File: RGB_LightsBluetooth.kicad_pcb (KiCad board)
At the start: 2 copper layers, 87.5 x 42.8 mm, 27 parts, among them J1 1935161, J2 1935161, J3 1935161, J4 HC-05, Q1 BC548, Q2 BC548, Q3 BC548, Q4 IRF9640, Q5 IRF9640, Q6 IRF9640, SW1 SW_DPST, U2 ATtiny2313-20P

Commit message: pcb without route
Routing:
- net GND: track 176.8 -> 0.00 mm
- net /12V: track 65.9 -> 0.00 mm
- net /5V: track 40.1 -> 0.00 mm
- net Net-(Q2-Pad1): track 26.3 -> 0.00 mm
- net Net-(Q1-Pad1): track 25.1 -> 0.00 mm
- net Net-(Q3-Pad1): track 24.9 -> 0.00 mm
- net Net-(J2-Pad1): track 21.6 -> 0.00 mm, vias 1 -> 0
- net Net-(J3-Pad1): track 21.1 -> 0.00 mm, vias 1 -> 0
- net Net-(J1-Pad1): track 20.6 -> 0.00 mm
- net /TX: track 18.5 -> 0.00 mm
- net Net-(J1-Pad2): track 17.9 -> 0.00 mm
- net /RX: track 17.5 -> 0.00 mm
- net Net-(R3-Pad2): track 14.3 -> 0.00 mm
- net Net-(Q1-Pad2): track 13.8 -> 0.00 mm
- net Net-(Q2-Pad2): track 13.1 -> 0.00 mm
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
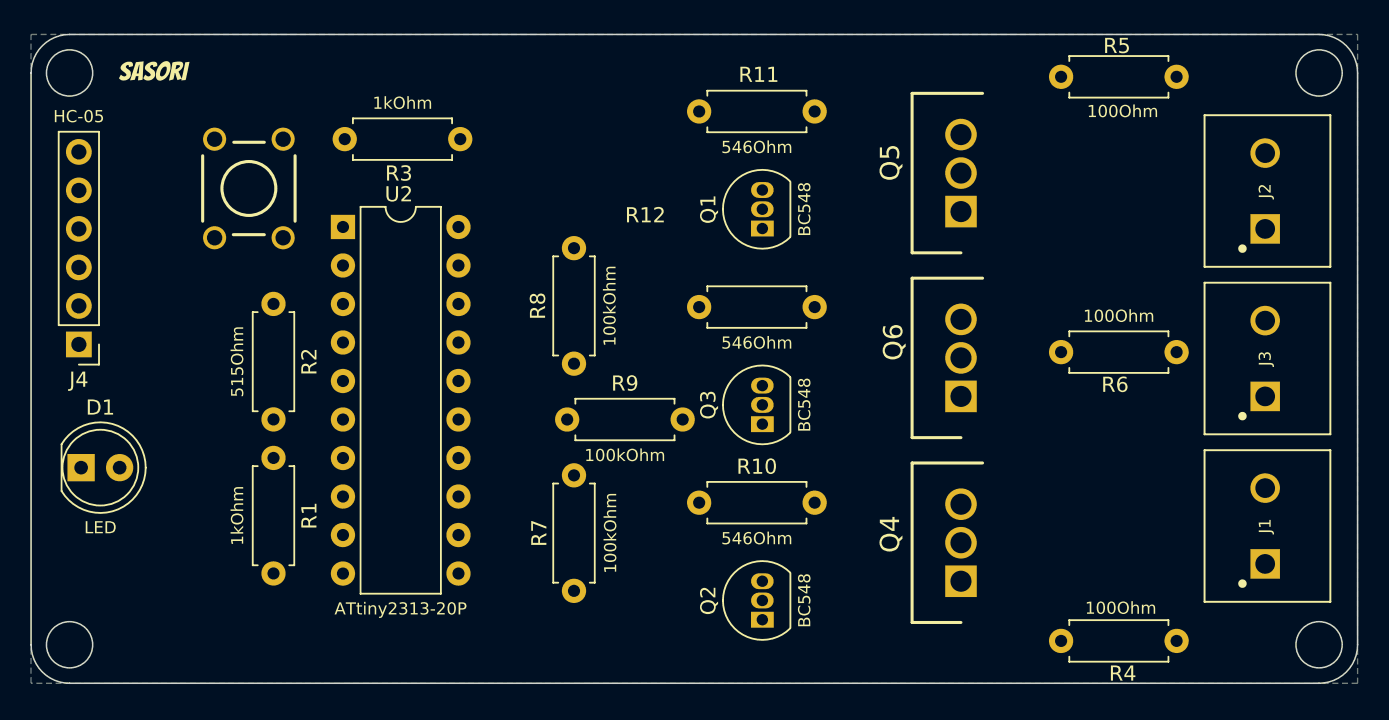
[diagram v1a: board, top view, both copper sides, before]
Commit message: pcb autorouting
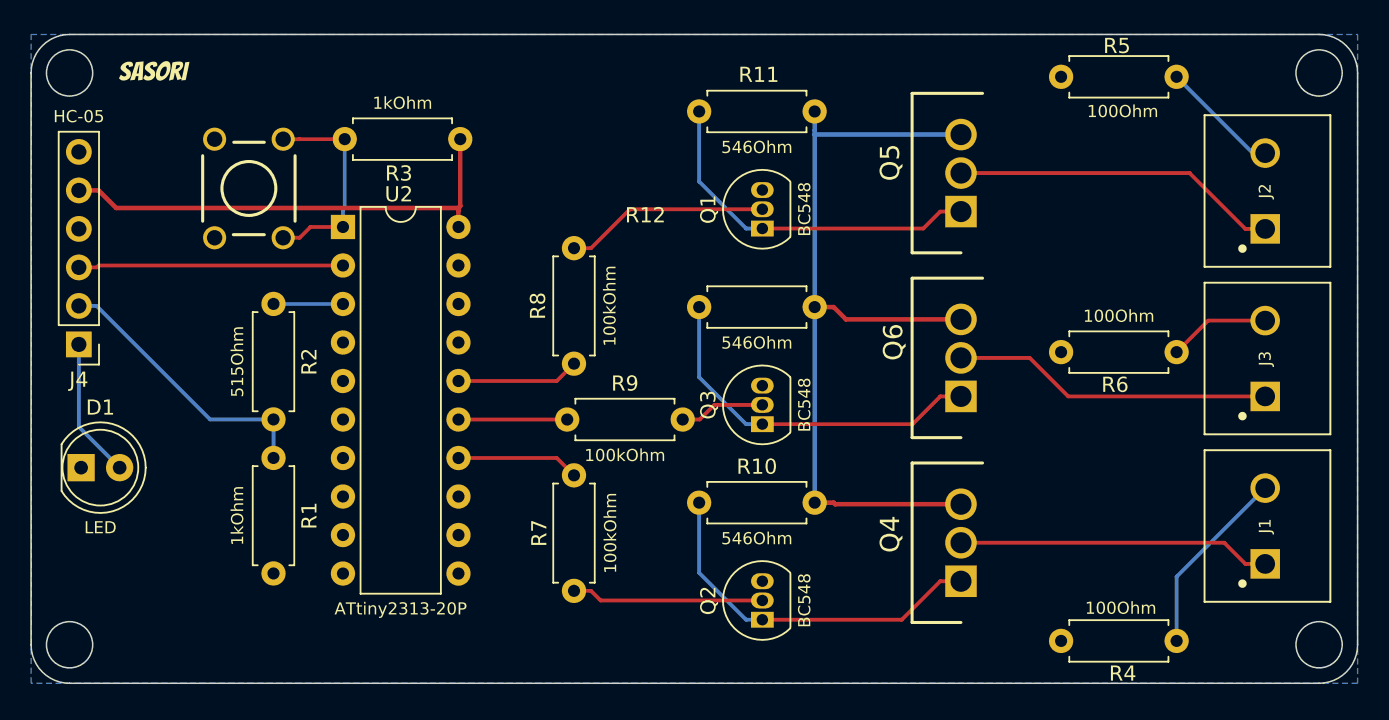
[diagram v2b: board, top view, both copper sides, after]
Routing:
- net /12V: track 0.00 -> 55.1 mm
- net /5V: track 0.00 -> 31.4 mm
- net Net-(Q2-Pad1): track 0.00 -> 24.2 mm
- net Net-(Q3-Pad1): track 0.00 -> 23.9 mm
- net Net-(Q1-Pad1): track 0.00 -> 23.6 mm
- net Net-(J2-Pad1): track 0.00 -> 21.6 mm
- net Net-(J3-Pad1): track 0.00 -> 21.1 mm
- net Net-(J1-Pad1): track 0.00 -> 20.6 mm
- net /TX: track 0.00 -> 18.5 mm
- net /RX: track 0.00 -> 17.5 mm
- net Net-(R3-Pad2): track 0.00 -> 14.1 mm
- net Net-(Q1-Pad2): track 0.00 -> 13.5 mm
- net Net-(Q2-Pad2): track 0.00 -> 12.7 mm
- net Net-(J1-Pad2): track 0.00 -> 12.5 mm
- net Net-(D1-Pad2): track 0.00 -> 9.24 mm
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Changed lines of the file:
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@@
     (style (thickness 0.1) (arrow_length 1.27) (text_position_mode 0) (extension_height 0.58642) (extension_offset 0.5) keep_text_aligned)
   )
+  (segment (start 136.261 71.9288) (end 133.2893 71.9288) (width 0.25) (layer "F.Cu") (net 2))
+  (segment (start 136.144 77.724) (end 133.9965 77.724) (width 0.25) (layer "F.Cu") (net 2))
+  (segment (start 132.198 71.9328) (end 133.2853 71.9328) (width 0.25) (layer "F.Cu") (net 2))
+  (segment (start 133.9965 77.724) (end 133.2853 78.4352) (width 0.25) (layer "F.Cu") (net 2))
+  (segment (start 133.2893 71.9288) (end 133.2853 71.9328) (width 0.25) (layer "F.Cu") (net 2))
+  (segment (start 132.198 78.4352) (end 133.2853 78.4352) (width 0.25) (layer "F.Cu") (net 2))
+  (segment (start 136.144 76.5987) (end 136.261 76.4817) (width 0.25) (layer "B.Cu") (net 2))
+  (segment (start 136.261 76.4817) (end 136.261 71.9288) (width 0.25) (layer "B.Cu") (net 2))
+  (segment (start 136.144 77.724) (end 136.144 76.5987) (width 0.25) (layer "B.Cu") (net 2))
+  (segment (start 118.722 82.931) (end 119.8973 82.931) (width 0.25) (layer "B.Cu") (net 3))
+  (segment (start 131.562 90.419) (end 127.3853 90.419) (width 0.25) (layer "B.Cu") (net 3))
+  (segment (start 131.562 90.419) (end 131.562 92.959) (width 0.25) (layer "B.Cu") (net 3))
+  (segment (start 127.3853 90.419) (end 119.8973 82.931) (width 0.25) (layer "B.Cu") (net 3))
+  (segment (start 131.567 82.804) (end 131.562 82.799) (width 0.25) (layer "B.Cu") (net 4))
+  (segment (start 136.144 82.804) (end 131.567 82.804) (width 0.25) (layer "B.Cu") (net 4))
+  (segment (start 143.881 76.3566) (end 143.881 71.9288) (width 0.3) (layer "F.Cu") (net 5))
+  (segment (start 118.722 75.311) (end 120.0223 75.311) (width 0.3) (layer "F.Cu") (net 5))
+  (segment (start 143.764 76.4736) (end 121.1849 76.4736) (width 0.3) (layer "F.Cu") (net 5))
+  (segment (start 143.764 77.724) (end 143.764 76.6238) (width 0.3) (layer "F.Cu") (net 5))
+  (segment (start 143.764 76.6238) (end 143.764 76.4736) (width 0.3) (layer "F.Cu") (net 5))
+  (segment (start 143.764 76.4736) (end 143.881 76.3566) (width 0.3) (layer "F.Cu") (net 5))
+  (segment (start 121.1849 76.4736) (end 120.0223 75.311) (width 0.3) (layer "F.Cu") (net 5))
+  (segment (start 196.977 94.949) (end 191.135 100.791) (width 0.25) (layer "B.Cu") (net 6))
+  (segment (start 191.135 100.791) (end 191.135 105.029) (width 0.25) (layer "B.Cu") (net 6))
+  (segment (start 196.168 72.851) (end 191.135 67.818) (width 0.25) (layer "B.Cu") (net 7))
+  (segment (start 196.977 72.851) (end 196.168 72.851) (width 0.25) (layer "B.Cu") (net 7))
+  (segment (start 196.977 83.9) (end 193.214 83.9) (width 0.25) (layer "F.Cu") (net 8))
+  (segment (start 193.214 83.9) (end 191.135 85.979) (width 0.25) (layer "F.Cu") (net 8))
+  (segment (start 143.764 92.964) (end 150.241 92.964) (width 0.25) (layer "F.Cu") (net 9))
+  (segment (start 150.241 92.964) (end 151.384 94.107) (width 0.25) (layer "F.Cu") (net 9))
+  (segment (start 153.1443 102.362) (end 152.5093 101.727) (width 0.25) (layer "F.Cu") (net 10))
+  (segment (start 151.384 101.727) (end 152.5093 101.727) (width 0.25) (layer "F.Cu") (net 10))
+  (segment (start 163.809 102.362) (end 153.1443 102.362) (width 0.25) (layer "F.Cu") (net 10))
+  (segment (start 143.764 87.884) (end 150.241 87.884) (width 0.25) (layer "F.Cu") (net 11))
+  (segment (start 150.241 87.884) (end 151.384 86.741) (width 0.25) (layer "F.Cu") (net 11))
+  (segment (start 151.384 79.121) (end 152.5093 79.121) (width 0.25) (layer "F.Cu") (net 12))
+  (segment (start 163.809 76.5556) (end 155.0747 76.5556) (width 0.25) (layer "F.Cu") (net 12))
+  (segment (start 155.0747 76.5556) (end 152.5093 79.121) (width 0.25) (layer "F.Cu") (net 12))
+  (segment (start 143.764 90.424) (end 150.934 90.424) (width 0.25) (layer "F.Cu") (net 13))
+  (segment (start 160.6445 89.4588) (end 163.809 89.4588) (width 0.25) (layer "F.Cu") (net 14))
+  (segment (start 158.554 90.424) (end 159.6793 90.424) (width 0.25) (layer "F.Cu") (net 14))
+  (segment (start 159.6793 90.424) (end 160.6445 89.4588) (width 0.25) (layer "F.Cu") (net 14))
+  (segment (start 175.5432 101.092) (end 173.0032 103.632) (width 0.25) (layer "F.Cu") (net 15))
+  (segment (start 173.0032 103.632) (end 163.809 103.632) (width 0.25) (layer "F.Cu") (net 15))
+  (segment (start 176.911 101.092) (end 175.5432 101.092) (width 0.25) (layer "F.Cu") (net 15))
+  (segment (start 162.7337 103.632) (end 159.639 100.5373) (width 0.25) (layer "B.Cu") (net 15))
+  (segment (start 163.809 103.632) (end 162.7337 103.632) (width 0.25) (layer "B.Cu") (net 15))
+  (segment (start 159.639 100.5373) (end 159.639 95.9104) (width 0.25) (layer "B.Cu") (net 15))
+  (segment (start 168.6109 96.012) (end 168.5093 95.9104) (width 0.3) (layer "F.Cu") (net 16))
+  (segment (start 176.911 83.82) (end 169.3221 83.82) (width 0.3) (layer "F.Cu") (net 16))
+  (segment (start 176.911 96.012) (end 168.6109 96.012) (width 0.3) (layer "F.Cu") (net 16))
+  (segment (start 167.259 95.9104) (end 168.5093 95.9104) (width 0.3) (layer "F.Cu") (net 16))
+  (segment (start 169.3221 83.82) (end 168.5093 83.0072) (width 0.3) (layer "F.Cu") (net 16))
+  (segment (start 167.259 83.0072) (end 168.5093 83.0072) (width 0.3) (layer "F.Cu") (net 16))
+  (segment (start 167.259 71.628) (end 167.259 71.3543) (width 0.3) (layer "B.Cu") (net 16))
+  (segment (start 167.259 70.104) (end 167.259 71.3543) (width 0.3) (layer "B.Cu") (net 16))
+  (segment (start 167.259 83.0072) (end 167.259 71.628) (width 0.3) (layer "B.Cu") (net 16))
+  (segment (start 167.259 95.9104) (end 167.259 83.0072) (width 0.3) (layer "B.Cu") (net 16))
+  (segment (start 167.259 71.628) (end 176.911 71.628) (width 0.3) (layer "B.Cu") (net 16))
+  (segment (start 174.4256 77.8256) (end 163.809 77.8256) (width 0.25) (layer "F.Cu") (net 17))
+  (segment (start 175.5432 76.708) (end 174.4256 77.8256) (width 0.25) (layer "F.Cu") (net 17))
+  (segment (start 176.911 76.708) (end 175.5432 76.708) (width 0.25) (layer "F.Cu") (net 17))
+  (segment (start 162.7337 77.8256) (end 159.639 74.7309) (width 0.25) (layer "B.Cu") (net 17))
+  (segment (start 163.809 77.8256) (end 162.7337 77.8256) (width 0.25) (layer "B.Cu") (net 17))
+  (segment (start 159.639 74.7309) (end 159.639 70.104) (width 0.25) (layer "B.Cu") (net 17))
+  (segment (start 175.5432 88.9) (end 173.7144 90.7288) (width 0.25) (layer "F.Cu") (net 18))
+  (segment (start 176.911 88.9) (end 175.5432 88.9) (width 0.25) (layer "F.Cu") (net 18))
+  (segment (start 173.7144 90.7288) (end 163.809 90.7288) (width 0.25) (layer "F.Cu") (net 18))
+  (segment (start 159.639 87.6341) (end 159.639 83.0072) (width 0.25) (layer "B.Cu") (net 18))
+  (segment (start 162.7337 90.7288) (end 159.639 87.6341) (width 0.25) (layer "B.Cu") (net 18))
+  (segment (start 163.809 90.7288) (end 162.7337 90.7288) (width 0.25) (layer "B.Cu") (net 18))
+  (segment (start 136.144 80.264) (end 120.0243 80.264) (width 0.25) (layer "F.Cu") (net 19))
+  (segment (start 120.0243 80.264) (end 119.8973 80.391) (width 0.25) (layer "F.Cu") (net 19))
+  (segment (start 118.722 80.391) (end 119.8973 80.391) (width 0.25) (layer "F.Cu") (net 19))
+  (segment (start 118.722 90.909) (end 121.412 93.599) (width 0.25) (layer "B.Cu") (net 32))
+  (segment (start 118.722 85.471) (end 118.722 90.909) (width 0.25) (layer "B.Cu") (net 32))
+  (segment (start 195.6767 99.949) (end 194.2797 98.552) (width 0.25) (layer "F.Cu") (net 33))
+  (segment (start 194.2797 98.552) (end 176.911 98.552) (width 0.25) (layer "F.Cu") (net 33))
+  (segment (start 196.977 99.949) (end 195.6767 99.949) (width 0.25) (layer "F.Cu") (net 33))
+  (segment (start 195.6767 77.851) (end 191.9937 74.168) (width 0.25) (layer "F.Cu") (net 34))
+  (segment (start 196.977 77.851) (end 195.6767 77.851) (width 0.25) (layer "F.Cu") (net 34))
+  (segment (start 191.9937 74.168) (end 176.911 74.168) (width 0.25) (layer "F.Cu") (net 34))
+  (segment (start 176.911 86.36) (end 181.444 86.36) (width 0.25) (layer "F.Cu") (net 35))
+  (segment (start 181.444 86.36) (end 183.984 88.9) (width 0.25) (layer "F.Cu") (net 35))
+  (segment (start 183.984 88.9) (end 196.977 88.9) (width 0.25) (layer "F.Cu") (net 35))
   (zone (net 1) (net_name "GND") (layer "B.Cu") (hatch edge 0.508)
     (connect_pads (clearance 0.508))
